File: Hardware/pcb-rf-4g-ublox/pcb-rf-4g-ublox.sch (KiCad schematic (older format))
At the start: 80 parts

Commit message: Annotate components
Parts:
- gave numbers to parts that had none: 80

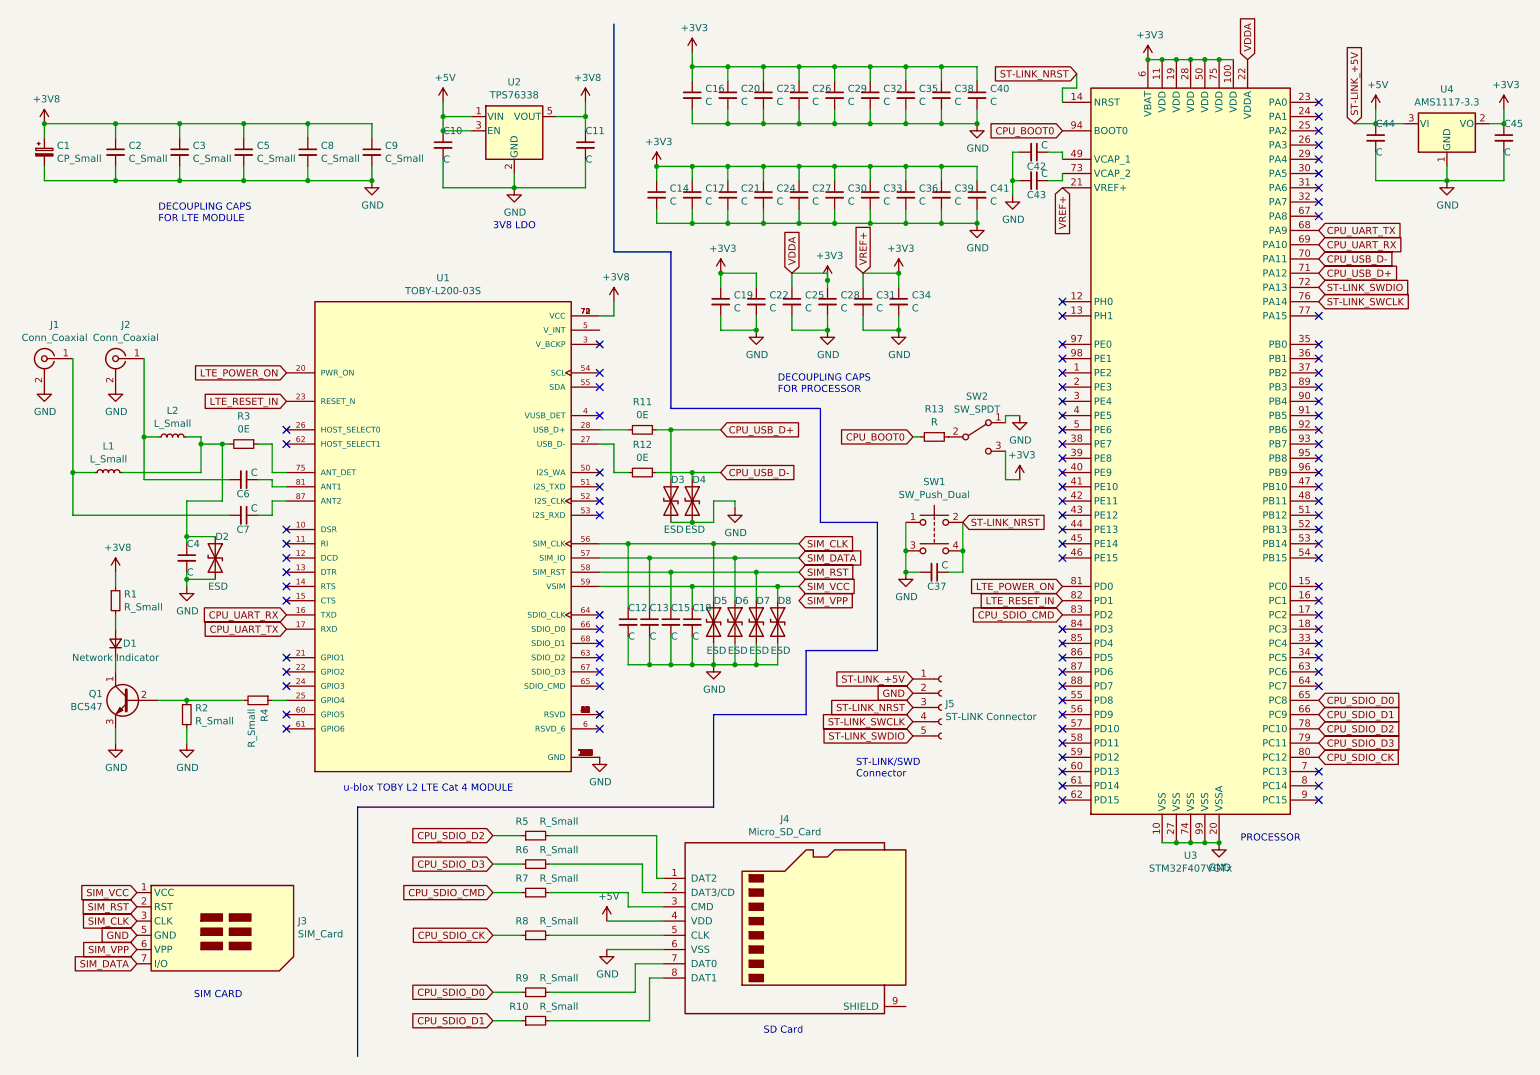
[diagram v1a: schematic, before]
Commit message: Split schematic into multiple files
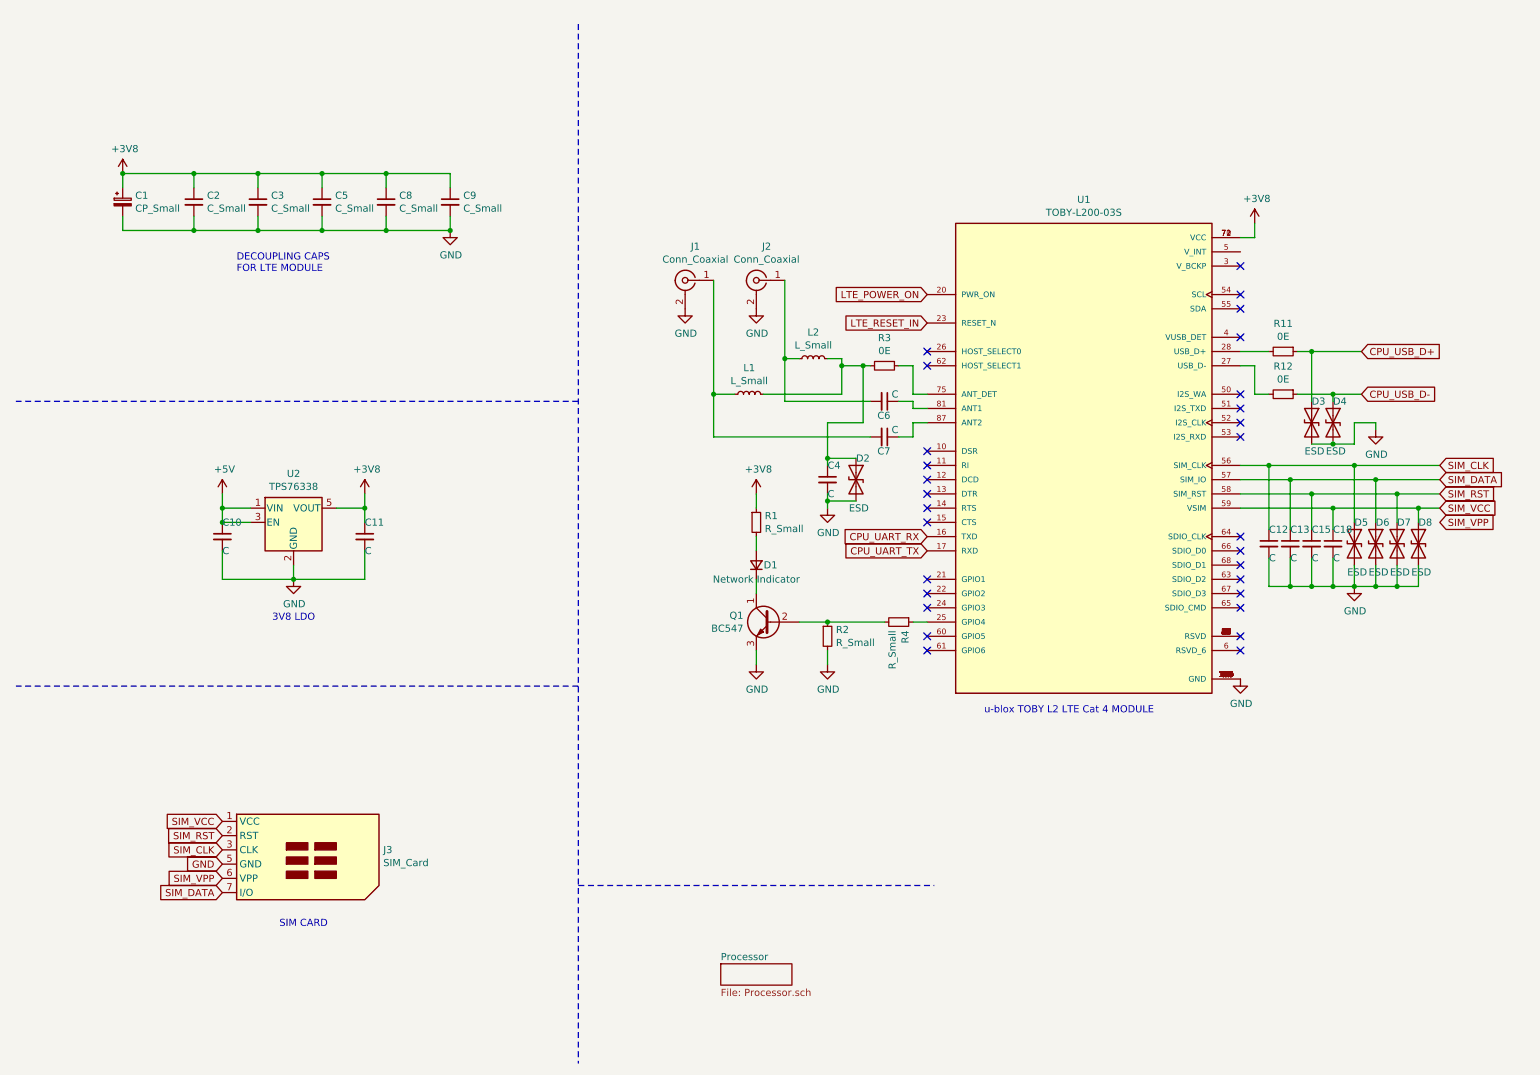
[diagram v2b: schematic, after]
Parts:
- removed C14, C16, C17, C19, C20, C21, C22, C23, C24, C25, C26, C27, C28, C29, C30, C31, C32, C33, C34, C35, C36, C37, C38, C39, C40, C41, C42, C43, C44, C45: C, symbol Device:C_Small
- removed J4: Micro_SD_Card, symbol Connector:Micro_SD_Card
- removed J5: ST-LINK Connector, symbol Connector:Conn_01x05_Female
- removed R10, R5, R6, R7, R8, R9: R_Small, symbol Device:R_Small
- removed R13: R, symbol Device:R_Small
- removed SW1: SW_Push_Dual, symbol Switch:SW_Push_Dual
- removed SW2: SW_SPDT, symbol Switch:SW_SPDT
- removed U3: STM32F407VGTx, Package_QFP:LQFP-100_14x14mm_P0.5mm, symbol MCU_ST_STM32F4:STM32F407VGTx
- removed U4: AMS1117-3.3, Package_TO_SOT_SMD:SOT-223-3_TabPin2, symbol Regulator_Linear:AMS1117-3.3
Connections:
- no-connect marks 97 -> 29
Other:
- note removed: "DECOUPLING CAPS\nFOR PROCESSOR"
- note removed: "PROCESSOR"
- note removed: "SD Card"
- note removed: "ST-LINK/SWD\nConnector"
- moved on the sheet: C1, C10, C11, C12, C13, C15, C18, C2, C3, C4, C5, C6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

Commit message: Assign values to the components
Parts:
- C1: value CP_Small -> 330uF
- C10: value C -> 10uF
- C11: value C -> 1000uF
- C12, C13, C15: value C -> 47pF
- C18: value C -> 100nF
- C2: value C_Small -> 100nF
- C3: value C_Small -> 10nF
- C5: value C_Small -> 68pF
- C6, C7: value C -> 33pF
- C8: value C_Small -> 15pF
- C9: value C_Small -> 6.2pF
- D1: value Network Indicator -> Network Indicator LED
- J1, J2: value Conn_Coaxial -> Male U.FL connector
- L1, L2: value L_Small -> 82nH
- R1, R2, R4: value R_Small -> R
- U1: footprint MODULE_TOBY-L200-03S -> SnapEDA:MODULE_TOBY-L200-03S
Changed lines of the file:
@@
 F 0 "U1" H 8000 5267 50  0000 C CNN
 F 1 "TOBY-L200-03S" H 8000 5176 50  0000 C CNN
-F 2 "MODULE_TOBY-L200-03S" H 8000 3500 50  0001 L BNN
+F 2 "SnapEDA:MODULE_TOBY-L200-03S" H 8000 3500 50  0001 L BNN
 F 3 "" H 8000 3500 50  0001 L BNN
 F 4 "U-Blox America Inc." H 8000 3500 50  0001 L BNN "MANUFACTURER"
@@
 P 1250 1750
 F 0 "C1" H 1338 1796 50  0000 L CNN
-F 1 "CP_Small" H 1338 1705 50  0000 L CNN
+F 1 "330uF" H 1338 1705 50  0000 L CNN
 F 2 "" H 1250 1750 50  0001 C CNN
 F 3 "~" H 1250 1750 50  0001 C CNN
@@
 P 1750 1750
 F 0 "C2" H 1842 1796 50  0000 L CNN
-F 1 "C_Small" H 1842 1705 50  0000 L CNN
+F 1 "100nF" H 1842 1705 50  0000 L CNN
 F 2 "" H 1750 1750 50  0001 C CNN
 F 3 "~" H 1750 1750 50  0001 C CNN
@@
 P 2200 1750
 F 0 "C3" H 2292 1796 50  0000 L CNN
-F 1 "C_Small" H 2292 1705 50  0000 L CNN
+F 1 "10nF" H 2292 1705 50  0000 L CNN
 F 2 "" H 2200 1750 50  0001 C CNN
 F 3 "~" H 2200 1750 50  0001 C CNN
@@
 P 2650 1750
 F 0 "C5" H 2742 1796 50  0000 L CNN
-F 1 "C_Small" H 2742 1705 50  0000 L CNN
+F 1 "68pF" H 2742 1705 50  0000 L CNN
 F 2 "" H 2650 1750 50  0001 C CNN
 F 3 "~" H 2650 1750 50  0001 C CNN
@@
 P 3100 1750
 F 0 "C8" H 3192 1796 50  0000 L CNN
-F 1 "C_Small" H 3192 1705 50  0000 L CNN
+F 1 "15pF" H 3192 1705 50  0000 L CNN
 F 2 "" H 3100 1750 50  0001 C CNN
 F 3 "~" H 3100 1750 50  0001 C CNN
@@
 P 3550 1750
 F 0 "C9" H 3642 1796 50  0000 L CNN
-F 1 "C_Small" H 3642 1705 50  0000 L CNN
+F 1 "6.2pF" H 3642 1705 50  0000 L CNN
 F 2 "" H 3550 1750 50  0001 C CNN
 F 3 "~" H 3550 1750 50  0001 C CNN
@@
 P 5700 4000
 F 0 "R1" H 5759 4046 50  0000 L CNN
-F 1 "R_Small" H 5759 3955 50  0000 L CNN
+F 1 "R" H 5759 3955 50  0000 L CNN
 F 2 "" H 5700 4000 50  0001 C CNN
 F 3 "~" H 5700 4000 50  0001 C CNN
@@
 P 5700 4300
 F 0 "D1" V 5700 4200 50  0000 C CNN
-F 1 "Network Indicator" V 5600 4300 50  0000 C CNN
+F 1 "Network Indicator LED" V 5600 4300 50  0000 C CNN
 F 2 "" V 5700 4300 50  0001 C CNN
 F 3 "~" V 5700 4300 50  0001 C CNN
@@
 U 1 1 6156D1CE
 P 6700 4700
-F 0 "R4" H 6759 4746 50  0000 L CNN
-F 1 "R_Small" H 6759 4655 50  0000 L CNN
+F 0 "R4" V 6800 4700 50  0000 L CNN
+F 1 "R" V 6800 4600 50  0000 L CNN
 F 2 "" H 6700 4700 50  0001 C CNN
 F 3 "~" H 6700 4700 50  0001 C CNN
@@
 P 6200 4800
 F 0 "R2" H 6259 4846 50  0000 L CNN
-F 1 "R_Small" H 6259 4755 50  0000 L CNN
+F 1 "R" H 6250 4750 50  0000 L CNN
 F 2 "" H 6200 4800 50  0001 C CNN
 F 3 "~" H 6200 4800 50  0001 C CNN
@@
 P 9900 4150
 F 0 "D5" V 9750 4150 50  0000 L CNN
-F 1 "ESD" V 10100 4100 50  0000 L CNN
+F 1 "ESD" H 10050 4200 50  0000 L CNN
 F 2 "" H 9900 4150 50  0001 C CNN
 F 3 "~" H 9900 4150 50  0001 C CNN
@@
 U 1 1 61571FC6
 P 9300 4150
-F 0 "C12" H 9300 4250 50  0000 L CNN
-F 1 "C" H 9300 4050 50  0000 L CNN
+F 0 "C12" V 9350 4200 50  0000 L CNN
+F 1 "47pF" V 9350 3900 50  0000 L CNN
 F 2 "" H 9300 4150 50  0001 C CNN
 F 3 "~" H 9300 4150 50  0001 C CNN
@@
 U 1 1 615951E4
 P 9450 4150
-F 0 "C13" H 9450 4250 50  0000 L CNN
-F 1 "C" H 9450 4050 50  0000 L CNN
+F 0 "C13" V 9500 4200 50  0000 L CNN
+F 1 "47pF" V 9500 3900 50  0000 L CNN
 F 2 "" H 9450 4150 50  0001 C CNN
 F 3 "~" H 9450 4150 50  0001 C CNN
@@
 U 1 1 615953BE
 P 9600 4150
-F 0 "C15" H 9600 4250 50  0000 L CNN
-F 1 "C" H 9600 4050 50  0000 L CNN
+F 0 "C15" V 9650 4200 50  0000 L CNN
+F 1 "47pF" V 9650 3900 50  0000 L CNN
 F 2 "" H 9600 4150 50  0001 C CNN
 F 3 "~" H 9600 4150 50  0001 C CNN
@@
 U 1 1 615955EC
 P 9750 4150
-F 0 "C18" H 9750 4250 50  0000 L CNN
-F 1 "C" H 9750 4050 50  0000 L CNN
+F 0 "C18" V 9800 4200 50  0000 L CNN
+F 1 "100nF" V 9800 3850 50  0000 L CNN
 F 2 "" H 9750 4150 50  0001 C CNN
 F 3 "~" H 9750 4150 50  0001 C CNN
@@
 P 10050 4150
 F 0 "D6" V 9900 4150 50  0000 L CNN
-F 1 "ESD" V 10250 4100 50  0000 L CNN
+F 1 "ESD" H 10200 4200 50  0000 L CNN
 F 2 "" H 10050 4150 50  0001 C CNN
 F 3 "~" H 10050 4150 50  0001 C CNN
@@
 P 10200 4150
 F 0 "D7" V 10050 4150 50  0000 L CNN
-F 1 "ESD" V 10400 4100 50  0000 L CNN
+F 1 "ESD" H 10350 4200 50  0000 L CNN
 F 2 "" H 10200 4150 50  0001 C CNN
 F 3 "~" H 10200 4150 50  0001 C CNN
@@
 P 10350 4150
 F 0 "D8" V 10200 4150 50  0000 L CNN
-F 1 "ESD" V 10550 4100 50  0000 L CNN
+F 1 "ESD" H 10500 4200 50  0000 L CNN
 F 2 "" H 10350 4150 50  0001 C CNN
 F 3 "~" H 10350 4150 50  0001 C CNN
@@
 P 1950 4100
 F 0 "C10" H 1950 4200 50  0000 L CNN
-F 1 "C" H 1950 4000 50  0000 L CNN
+F 1 "10uF" H 1950 4000 50  0000 L CNN
 F 2 "" H 1950 4100 50  0001 C CNN
 F 3 "~" H 1950 4100 50  0001 C CNN
@@
 P 2950 4100
 F 0 "C11" H 2950 4200 50  0000 L CNN
-F 1 "C" H 2950 4000 50  0000 L CNN
+F 1 "1000uF" H 2950 4000 50  0000 L CNN
 F 2 "" H 2950 4100 50  0001 C CNN
 F 3 "~" H 2950 4100 50  0001 C CNN
@@
 P 6600 3150
 F 0 "C6" V 6700 3100 50  0000 L CNN
-F 1 "C" V 6550 3200 50  0000 L CNN
+F 1 "33pF" V 6450 3100 50  0000 L CNN
 F 2 "" H 6600 3150 50  0001 C CNN
 F 3 "~" H 6600 3150 50  0001 C CNN
@@
 P 6600 3400
 F 0 "C7" V 6700 3350 50  0000 L CNN
-F 1 "C" V 6550 3450 50  0000 L CNN
+F 1 "33pF" V 6800 3350 50  0000 L CNN
 F 2 "" H 6600 3400 50  0001 C CNN
 F 3 "~" H 6600 3400 50  0001 C CNN
@@
 P 5200 2300
 F 0 "J1" H 5128 2538 50  0000 C CNN
-F 1 "Conn_Coaxial" H 5128 2447 50  0000 C CNN
+F 1 "Male U.FL connector" V 5350 2350 50  0000 C CNN
 F 2 "" H 5200 2300 50  0001 C CNN
 F 3 " ~" H 5200 2300 50  0001 C CNN
@@
 P 5700 2300
 F 0 "J2" H 5628 2538 50  0000 C CNN
-F 1 "Conn_Coaxial" H 5628 2447 50  0000 C CNN
+F 1 "Male U.FL connector" V 5800 2400 50  0000 C CNN
 F 2 "" H 5700 2300 50  0001 C CNN
 F 3 " ~" H 5700 2300 50  0001 C CNN
@@
 P 5650 3100
 F 0 "L1" V 5835 3100 50  0000 C CNN
-F 1 "L_Small" V 5744 3100 50  0000 C CNN
+F 1 "82nH" V 5744 3100 50  0000 C CNN
 F 2 "" H 5650 3100 50  0001 C CNN
 F 3 "~" H 5650 3100 50  0001 C CNN
@@
 P 6100 2850
 F 0 "L2" V 6285 2850 50  0000 C CNN
-F 1 "L_Small" V 6194 2850 50  0000 C CNN
+F 1 "82nH" V 6194 2850 50  0000 C CNN
 F 2 "" H 6100 2850 50  0001 C CNN
 F 3 "~" H 6100 2850 50  0001 C CNN
